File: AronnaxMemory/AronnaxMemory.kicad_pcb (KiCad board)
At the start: 6 copper layers, 161.3 x 64.8 mm, 49 parts, among them J1 Barrel_Jack_Switch, J11 Conn_02x18_Odd_Even, J12 IRQ In, J2 Conn_02x40_Odd_Even, J3 Conn_02x18_Odd_Even, J8 RAM Select, J9 VP A1-A4, U10 AS6C4008-55PCN, U11 AS6C4008-55PCN, U12 AS6C4008-55PCN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

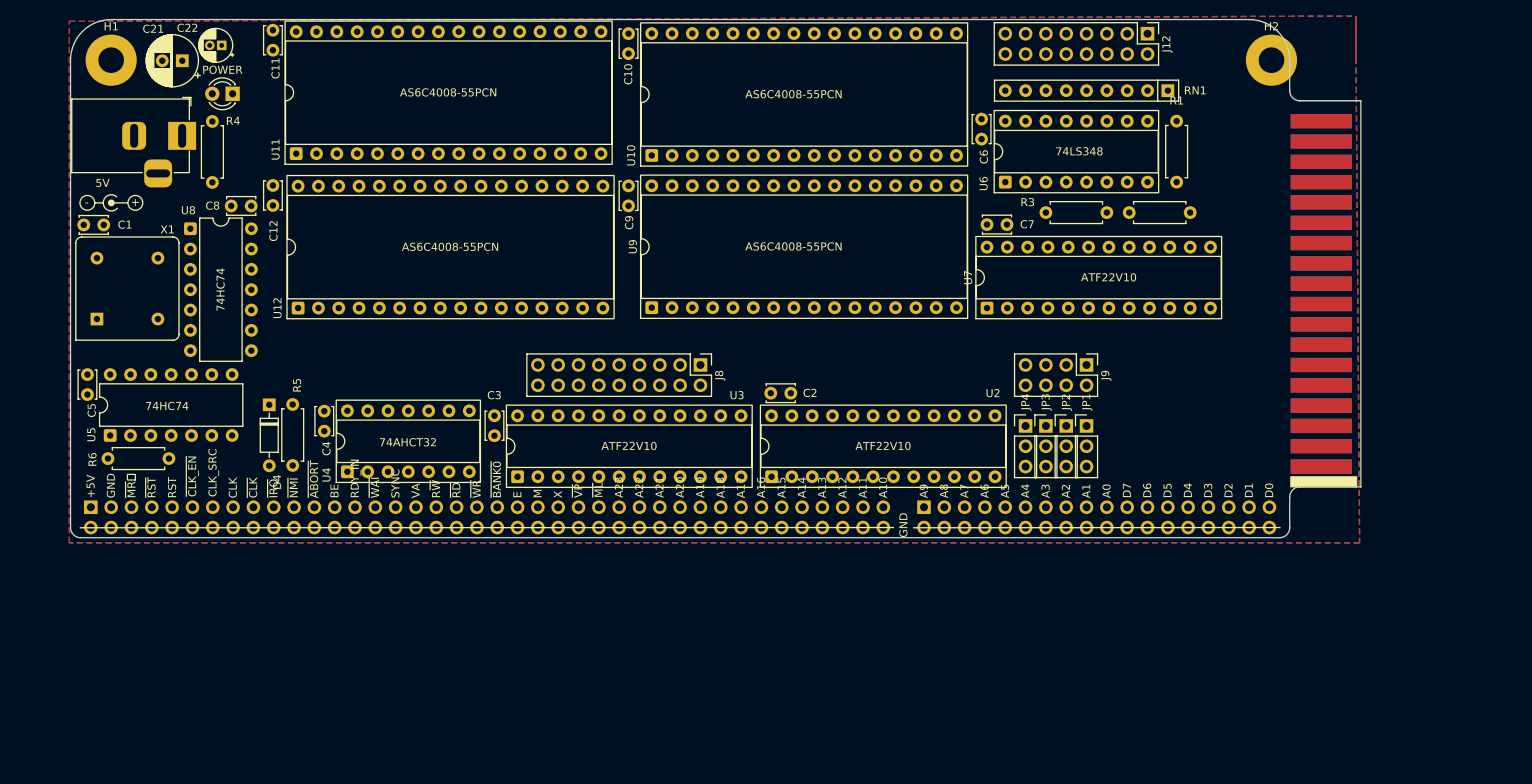
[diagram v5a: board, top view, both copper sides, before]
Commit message: Simplifying Removed VPR
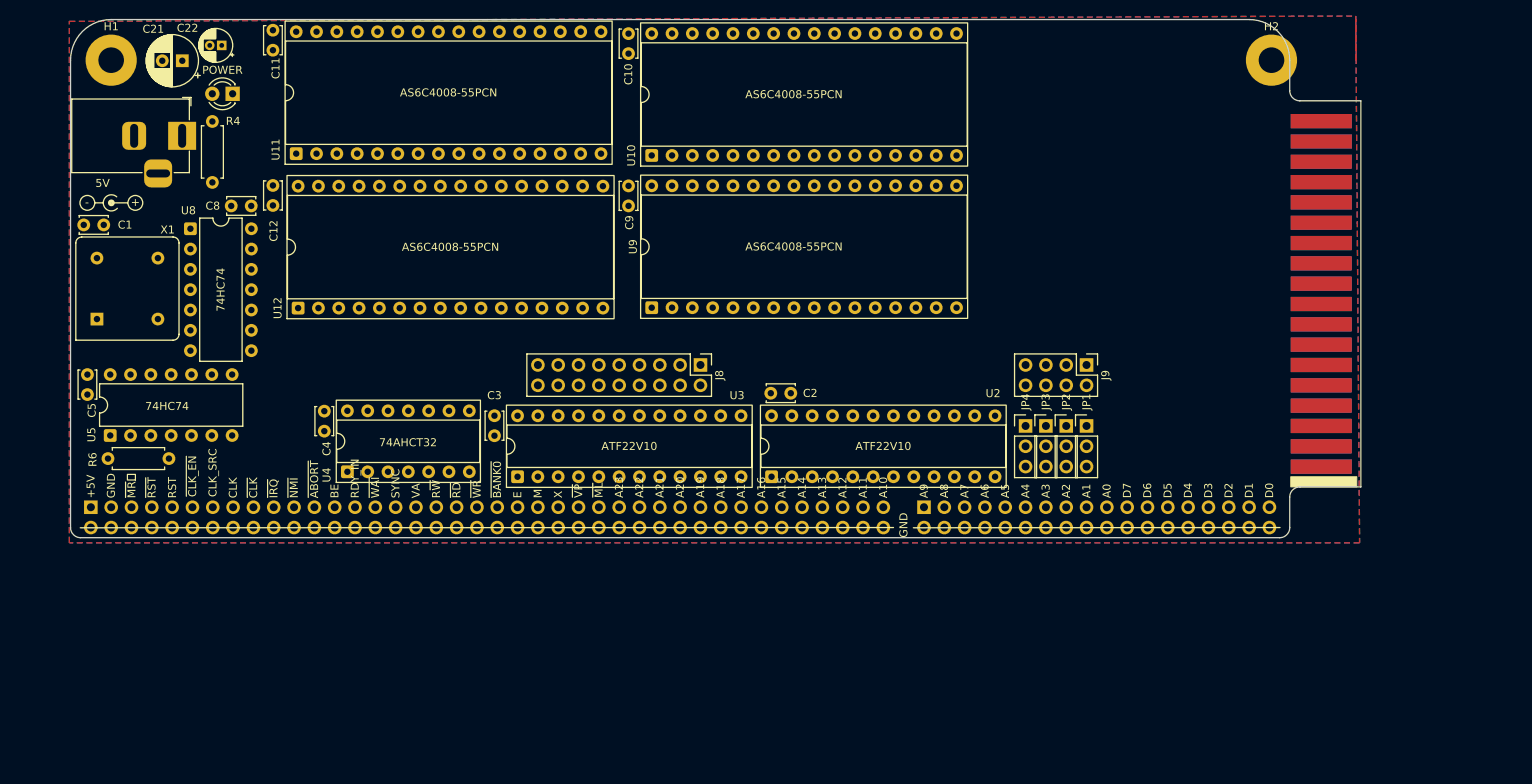
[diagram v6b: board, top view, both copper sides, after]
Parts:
- removed C6, C7: 100nF, Capacitor_THT:C_Disc_D3.4mm_W2.1mm_P2.50mm
- removed D4: 1N4148, Diode_THT:D_DO-35_SOD27_P7.62mm_Horizontal
- removed J12: IRQ In, Connector_PinHeader_2.54mm:PinHeader_2x08_P2.54mm_Vertical
- removed R1, R2, R3, R5: 10K, Resistor_THT:R_Axial_DIN0207_L6.3mm_D2.5mm_P7.62mm_Horizontal
- removed RN1: 100k, Resistor_THT:R_Array_SIP9
- removed U6: 74LS348, Package_DIP:DIP-16_W7.62mm_Socket
- removed U7: ATF22V10, Package_DIP:DIP-24_W7.62mm_Socket
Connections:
- net /~{2M_4} renamed /~{RAM_4}
- net /~{2M_5} renamed /~{RAM_5}
- net /~{2M_6} renamed /~{RAM_6}
- net /~{2M_7} renamed /~{RAM_7}
- J2 pad 53: /A21 -> /A23
- J2 pad 55: /A21 -> /A22
- J2 pad 59: /A21 -> /A20
- J2 pad 61: /A21 -> /A19
- J2 pad 63: /A21 -> /A18
- J2 pad 65: /A21 -> /A17
- J2 pad 67: /A21 -> /A16
- J8 pad 2: /~{2M_0} -> /~{RAM_0}
- J8 pad 4: /~{2M_1} -> /~{RAM_1}
- J8 pad 6: /~{2M_2} -> /~{RAM_2}
- J8 pad 8: /~{2M_3} -> /~{RAM_3}
- U10 pad 1: /A21 -> /A18
- U10 pad 2: /A21 -> /A16
- U10 pad 30: /A21 -> /A17
- U11 pad 1: /A21 -> /A18
- U11 pad 2: /A21 -> /A16
- U11 pad 30: /A21 -> /A17
- U12 pad 1: /A21 -> /A18
- U12 pad 2: /A21 -> /A16
- U12 pad 30: /A21 -> /A17
- U2 pad 22: /A21 -> /~{VPR}
- U3 pad 10: /A21 -> /A17
- U3 pad 11: /A21 -> /A16
- U3 pad 15: /~{2M_0} -> /~{RAM_0}
- U3 pad 16: /~{2M_1} -> /~{RAM_1}
- U3 pad 17: /~{2M_2} -> /~{RAM_2}
- U3 pad 18: /~{2M_3} -> /~{RAM_3}
- U3 pad 4: /A21 -> /A23
- U3 pad 5: /A21 -> /A22
- U3 pad 7: /A21 -> /A20
- U3 pad 8: /A21 -> /A19
- U3 pad 9: /A21 -> /A18
- U9 pad 1: /A21 -> /A18
- U9 pad 2: /A21 -> /A16
- U9 pad 30: /A21 -> /A17

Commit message: May 2025
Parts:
- removed C10, C11, C12, C8, C9: 100nF, Capacitor_THT:C_Disc_D3.4mm_W2.1mm_P2.50mm
- removed J9: VP A1-A4, Connector_PinHeader_2.54mm:PinHeader_2x04_P2.54mm_Vertical
- removed JP1, JP2, JP3, JP4: Jumper3_254mm, Jumper3_254mm:Jumper3_254mm
- removed U10, U11, U12, U9: AS6C4008-55PCN, Package_DIP:DIP-32_W15.24mm_Socket
- removed U8: 74HC74, Package_DIP:DIP-14_W7.62mm
- added C6: 100nF, Capacitor_THT:C_Disc_D3.4mm_W2.1mm_P2.50mm, F.Cu at (157.1, 100.5)
- added U6: 74HC74, Package_DIP:DIP-14_W7.62mm_Socket, F.Cu at (160.0, 108.2)
- J11: moved to F.Cu
- U5: footprint Package_DIP:DIP-14_W7.62mm -> Package_DIP:DIP-14_W7.62mm_Socket
- moved C5 125.4 mm to (152.7, 102.4), turned to 180 degrees
- moved U5 115.3 mm to (145.0, 105.3), turned to 0 degrees
- moved X1 102.5 mm to (131.1, 107.9)
- moved C1 100.2 mm to (127.0, 99.1), turned to -90 degrees
- moved U4 100.0 mm to (160.0, 120.7)
- moved C4 100.0 mm to (157.1, 113.1)
- moved J11 49.1 mm to (154.2, 136.5), turned to 0 degrees
- moved R4 14.4 mm to (53.1, 68.3), turned to 180 degrees
- moved D1 5.16 mm to (50.5, 73.7), turned to 0 degrees
- moved C22 4.54 mm to (45.5, 73.7), turned to 0 degrees
- moved H2 2.80 mm to (172.7, 71.1)
- moved REF** 2.60 mm to (29.5, 86.5)
- moved C2 2.54 mm to (112.9, 110.2)
- moved C3 2.54 mm to (78.4, 113.0)
- moved J8 2.54 mm to (104.1, 106.7)
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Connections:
- U2 pad 10: /A7 -> /A8
- U2 pad 11: /~{BANK0} -> /A7
- U2 pad 13: /~{VP} -> unconnected-(U2-I-Pad13)
- U2 pad 14: /E -> unconnected-(U2-O-Pad14)
- U2 pad 2: /A15 -> /~{BANK0}
- U2 pad 22: /~{VPR} -> unconnected-(U2-O-Pad22)
- U2 pad 3: /A14 -> /A15
- U2 pad 4: /A13 -> /A14
- U2 pad 5: /A12 -> /A13
- U2 pad 6: /A11 -> /A12
- U2 pad 7: /A10 -> /A11
- U2 pad 8: /A9 -> /A10
- U2 pad 9: /A8 -> /A9
- U3 pad 1: GND -> /~{RD}
- U3 pad 13: GND -> /IO_AREA
- U3 pad 2: /IO_AREA -> /E
- U3 pad 3: /~{RD} -> GND
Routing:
- net /~{RESET}: track 0.00 -> 152.2 mm, vias 0 -> 1
- net /~{IRQ}: track 0.00 -> 137.8 mm
- net /CLK_SRC: track 0.00 -> 133.2 mm
- net /~{NMI}: track 0.00 -> 127.0 mm, vias 0 -> 1
- net /R~{W}: track 0.00 -> 74.2 mm
- net /~{IOREADY}: track 0.00 -> 57.0 mm
- net /IOWAIT: track 0.00 -> 50.6 mm, vias 0 -> 1
- net /IO_AREA: track 0.00 -> 46.3 mm
- net /~{BANK0}: track 0.00 -> 39.5 mm
- net /A7: track 0.00 -> 37.8 mm, vias 0 -> 1
- net /A14: track 0.00 -> 36.4 mm
- net /A13: track 0.00 -> 35.1 mm
- net /D0: track 0.00 -> 33.9 mm, vias 0 -> 1
- net /D3: track 0.00 -> 32.9 mm, vias 0 -> 1
- net /DCLK: track 0.00 -> 32.2 mm
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- added copper zone on In3.Cu, net GND
- added copper zone on In4.Cu, net GND
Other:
- board size 161.3 x 64.8 mm -> 152.4 x 81.6 mm
